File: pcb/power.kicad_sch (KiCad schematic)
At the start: 17 parts, among them Q1 CSD18540Q5B, U1 LM74500-Q1, U2 TVS2700DRV, U3 TPSM33620S5QRDNRQ1, U4 LM1117-Q1-3.3

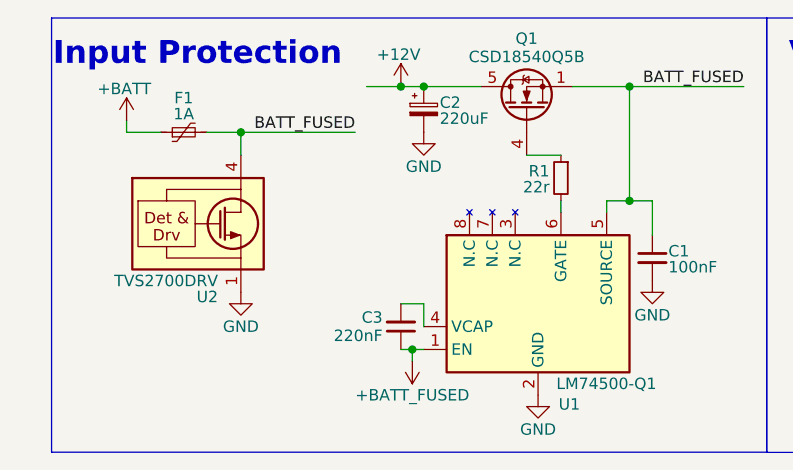
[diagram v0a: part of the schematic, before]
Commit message: pcb gitignore update, netting and mcu pinning
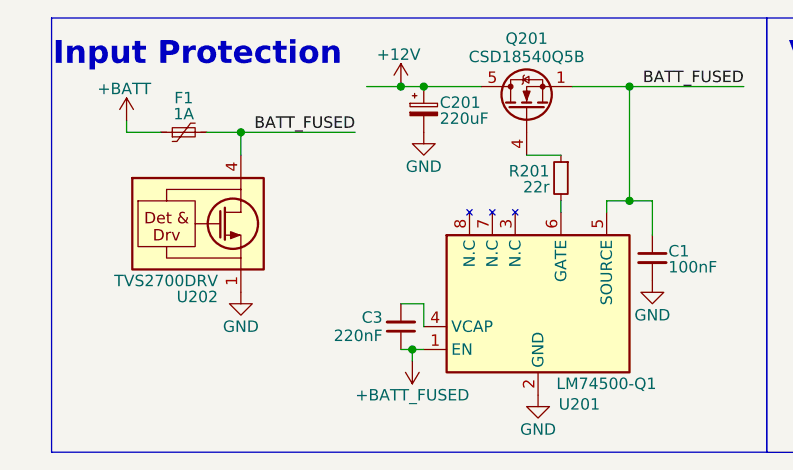
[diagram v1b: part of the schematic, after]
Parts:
- renumbered C2 to C201, Q1 to Q201, R1 to R201, U1 to U201, U2 to U202
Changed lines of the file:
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@@
 		(on_board yes)
 		(dnp no)
-		(property "Reference" "U2"
+		(property "Reference" "U202"
 			(at 33.02 44.958 0)
 			(effects
@@
 			(project "kh_obd2_interface"
 				(path "/0736e313-8db4-41af-b70d-53af7104d2ca/3f40c237-d495-44df-82aa-7228d577e747"
-					(reference "U2")
+					(reference "U202")
 					(unit 1)
 				)
@@
 		(on_board yes)
 		(dnp no)
-		(property "Reference" "R1"
+		(property "Reference" "R201"
 			(at 69.85 30.988 0)
 			(effects
@@
 			(project "kh_obd2_interface"
 				(path "/0736e313-8db4-41af-b70d-53af7104d2ca/3f40c237-d495-44df-82aa-7228d577e747"
-					(reference "R1")
+					(reference "R201")
 					(unit 1)
 				)
@@
 		(on_board yes)
 		(dnp no)
-		(property "Reference" "Q1"
+		(property "Reference" "Q201"
 			(at 67.31 16.256 90)
 			(effects
@@
 			(project "kh_obd2_interface"
 				(path "/0736e313-8db4-41af-b70d-53af7104d2ca/3f40c237-d495-44df-82aa-7228d577e747"
-					(reference "Q1")
+					(reference "Q201")
 					(unit 1)
 				)
@@
 		(on_board yes)
 		(dnp no)
-		(property "Reference" "U1"
+		(property "Reference" "U201"
 			(at 70.866 56.896 0)
 			(effects
@@
 			(project "kh_obd2_interface"
 				(path "/0736e313-8db4-41af-b70d-53af7104d2ca/3f40c237-d495-44df-82aa-7228d577e747"
-					(reference "U1")
+					(reference "U201")
 					(unit 1)
 				)
@@
 		(on_board yes)
 		(dnp no)
-		(property "Reference" "C2"
+		(property "Reference" "C201"
 			(at 57.658 23.368 0)
 			(effects
@@
 			(project "kh_obd2_interface"
 				(path "/0736e313-8db4-41af-b70d-53af7104d2ca/3f40c237-d495-44df-82aa-7228d577e747"
-					(reference "C2")
-					(unit 1)
-				)
+					(reference "C201")
+					(unit 1)
+				)

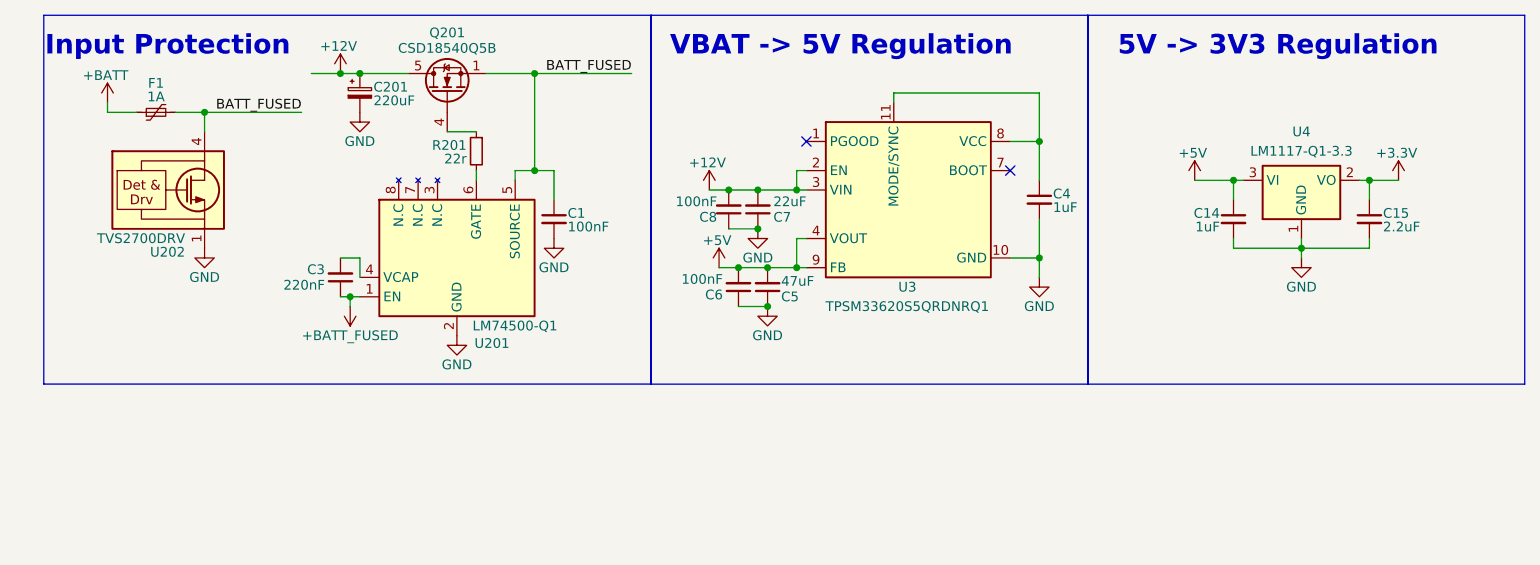
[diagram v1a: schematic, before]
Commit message: add transceivers, routing, drc
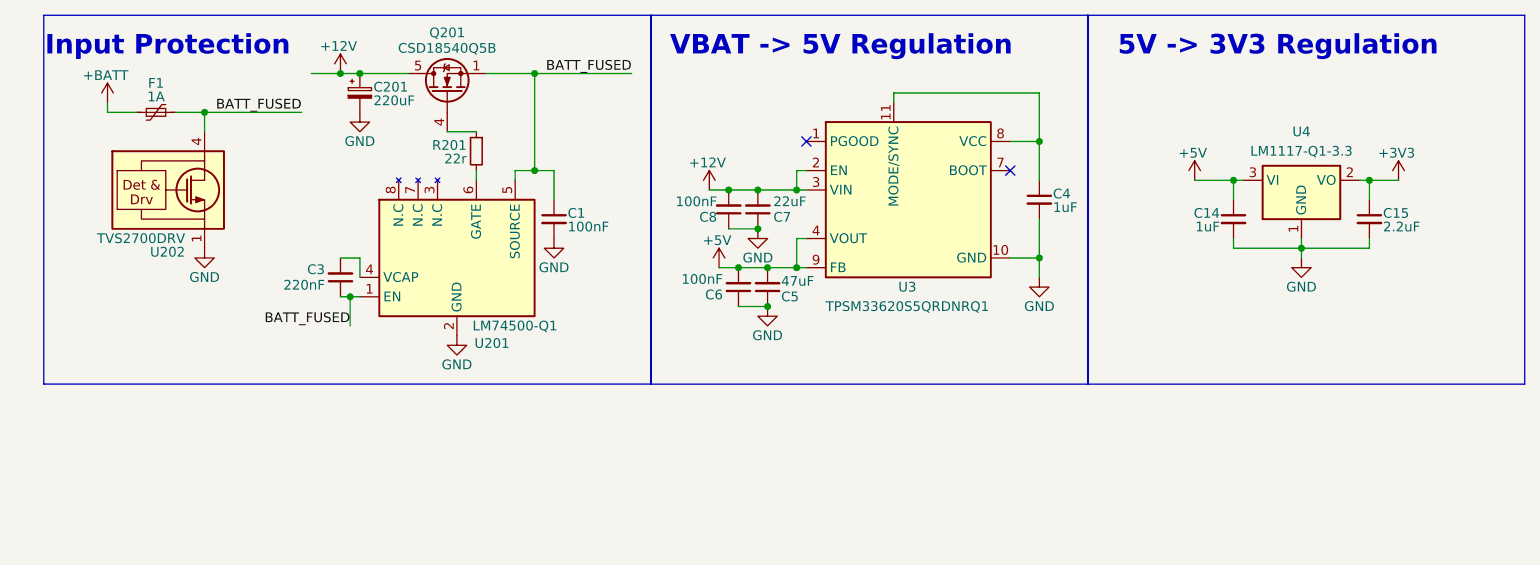
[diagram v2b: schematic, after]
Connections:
- net +BATT_FUSED is gone; now on net BATT_FUSED: C3.1, U201.1 (EN)
- net +3.3V renamed +3V3
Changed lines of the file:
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@@
 	(wire
 		(pts
-			(xy 54.61 50.8) (xy 54.61 52.07)
+			(xy 54.61 50.8) (xy 54.61 54.61)
 		)
 		(stroke
@@
 		)
 	)
+	(label "BATT_FUSED"
+		(at 54.61 54.61 180)
+		(effects
+			(font
+				(size 1.27 1.27)
+			)
+			(justify right bottom)
+		)
+	)
 	(symbol
 		(lib_id "Device:C_Small")
@@
 	(symbol
 		(lib_id "power:+BATT")
-		(at 54.61 52.07 180)
-		(unit 1)
-		(exclude_from_sim no)
-		(in_bom yes)
-		(on_board yes)
-		(dnp no)
-		(property "Reference" "#PWR05"
-			(at 54.61 48.26 0)
-			(effects
-				(font
-					(size 1.27 1.27)
-				)
-				(hide yes)
-			)
-		)
-		(property "Value" "+BATT_FUSED"
-			(at 54.61 55.88 0)
-			(effects
-				(font
-					(size 1.27 1.27)
-				)
-			)
-		)
-		(property "Footprint" ""
-			(at 54.61 52.07 0)
-			(effects
-				(font
-					(size 1.27 1.27)
-				)
-				(hide yes)
-			)
-		)
-		(property "Datasheet" ""
-			(at 54.61 52.07 0)
-			(effects
-				(font
-					(size 1.27 1.27)
-				)
-				(hide yes)
-			)
-		)
-		(property "Description" "Power symbol creates a global label with name \"+BATT\""
-			(at 54.61 52.07 0)
-			(effects
-				(font
-					(size 1.27 1.27)
-				)
-				(hide yes)
-			)
-		)
-		(pin "1"
-		)
-		(instances
-			(project "kh_obd2_interface"
-				(path "/0736e313-8db4-41af-b70d-53af7104d2ca/3f40c237-d495-44df-82aa-7228d577e747"
-					(reference "#PWR05")
-					(unit 1)
-				)
-			)
-		)
-	)
-	(symbol
-		(lib_id "power:+BATT")
 		(at 101.6 36.83 0)
 		(unit 1)
@@
 			)
 		)
-		(property "Value" "+3.3V"
+		(property "Value" "+3V3"
 			(at 191.516 32.004 0)
 			(effects

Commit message: busses are hard
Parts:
- added SW2: SW_SPDT, Connector_PinHeader_2.54mm:PinHeader_1x03_P2.54mm_Vertical_SMD_Pin1Left, symbol Switch:SW_SPDT
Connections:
- net +5V: now also SW2.2 (B); no longer C5.2, C6.2, U3.4 (VOUT), U3.9 (FB)
- new net CAR_5V: C5.2, C6.2, SW2.1 (A), U3.4 (VOUT), U3.9 (FB)
- new net USB_5V: SW2.3 (C)
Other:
- note added: "5V Sourcing Switch"
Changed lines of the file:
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@@
 	(rectangle
 		(start 93.98 13.97)
-		(end 151.1299 62.2299)
+		(end 151.1299 62.23)
 		(stroke
 			(width 0)
@@
 	)
 	(rectangle
-		(start 14.5249 13.97)
-		(end 93.98 62.2151)
+		(start 14.605 13.97)
+		(end 93.98 62.23)
 		(stroke
 			(width 0)
@@
 		(start 151.13 13.97)
 		(end 208.2799 62.2299)
+		(stroke
+			(width 0)
+			(type default)
+		)
+		(fill
+			(type none)
+		)
+	)
+	(rectangle
+		(start 14.605 62.23)
+		(end 54.6099 83.8199)
 		(stroke
 			(width 0)
@@
 		)
 	)
+	(text "5V Sourcing Switch"
+		(exclude_from_sim no)
+		(at 35.052 66.04 0)
+		(effects
+			(font
+				(size 2.54 2.54)
+				(thickness 0.508)
+				(bold yes)
+			)
+		)
+	)
 	(text "Input Protection"
 		(exclude_from_sim no)
@@
 	)
 	(junction
-		(at 53.34 21.59)
-		(diameter 0)
-		(color 0 0 0 0)
-	)
-	(junction
 		(at 113.03 36.83)
 		(diameter 0)
@@
 	(wire
 		(pts
+			(xy 96.52 46.99) (xy 105.41 46.99)
+		)
+		(stroke
+			(width 0)
+			(type default)
+		)
+	)
+	(wire
+		(pts
+			(xy 43.18 73.66) (xy 43.18 77.47)
+		)
+		(stroke
+			(width 0)
+			(type default)
+		)
+	)
+	(wire
+		(pts
 			(xy 53.34 21.59) (xy 55.88 21.59)
 		)
@@
 	(wire
 		(pts
+			(xy 35.56 46.99) (xy 35.56 44.45)
+		)
+		(stroke
+			(width 0)
+			(type default)
+		)
+	)
+	(wire
+		(pts
 			(xy 186.69 35.56) (xy 187.96 35.56)
 		)
@@
 	(wire
 		(pts
-			(xy 102.87 46.99) (xy 105.41 46.99)
+			(xy 26.67 74.93) (xy 29.21 74.93)
 		)
 		(stroke
@@
 	(wire
 		(pts
-			(xy 49.53 21.59) (xy 53.34 21.59)
+			(xy 21.59 80.01) (xy 29.21 80.01)
 		)
 		(stroke
@@
 		(pts
 			(xy 53.34 50.8) (xy 54.61 50.8)
+		)
+		(stroke
+			(width 0)
+			(type default)
+		)
+	)
+	(wire
+		(pts
+			(xy 39.37 77.47) (xy 43.18 77.47)
 		)
 		(stroke
@@
 		)
 	)
+	(label "CAR_5V"
+		(at 96.52 46.99 0)
+		(effects
+			(font
+				(size 1.27 1.27)
+			)
+			(justify left bottom)
+		)
+	)
+	(label "CAR_5V"
+		(at 21.59 80.01 0)
+		(effects
+			(font
+				(size 1.27 1.27)
+			)
+			(justify left bottom)
+		)
+	)
 	(label "BATT_FUSED"
 		(at 48.26 26.67 180)
@@
 		)
 	)
+	(hierarchical_label "USB_5V"
+		(shape input)
+		(at 26.67 74.93 180)
+		(effects
+			(font
+				(size 1.27 1.27)
+			)
+			(justify right)
+		)
+	)
 	(symbol
 		(lib_id "Device:C_Small")
@@
 	(symbol
 		(lib_id "power:+BATT")
-		(at 102.87 46.99 0)
+		(at 43.18 73.66 0)
 		(unit 1)
 		(exclude_from_sim no)
@@
 		(dnp no)
 		(property "Reference" "#PWR019"
-			(at 102.87 50.8 0)
+			(at 43.18 77.47 0)
 			(effects
 				(font
@@
 		)
 		(property "Value" "+5V"
-			(at 102.616 43.434 0)
+			(at 42.926 70.104 0)
 			(effects
 				(font
@@
 		)
 		(property "Footprint" ""
-			(at 102.87 46.99 0)
+			(at 43.18 73.66 0)
 			(effects
 				(font
@@
 		)
 		(property "Datasheet" ""
-			(at 102.87 46.99 0)
+			(at 43.18 73.66 0)
 			(effects
 				(font
@@
 		)
 		(property "Description" "Power symbol creates a global label with name \"+BATT\""
-			(at 102.87 46.99 0)
+			(at 43.18 73.66 0)
 			(effects
 				(font
@@
 	(symbol
 		(lib_id "power:GND")
-		(at 35.56 44.45 0)
+		(at 35.56 46.99 0)
 		(unit 1)
 		(exclude_from_sim no)
@@
 		(dnp no)
 		(property "Reference" "#PWR03"
+			(at 35.56 53.34 0)
+			(effects
+				(font
+					(size 1.27 1.27)
+				)
+				(hide yes)
+			)
+		)
+		(property "Value" "GND"
 			(at 35.56 50.8 0)
 			(effects
@@
 					(size 1.27 1.27)
 				)
-				(hide yes)
-			)
-		)
-		(property "Value" "GND"
-			(at 35.56 48.26 0)
-			(effects
-				(font
-					(size 1.27 1.27)
-				)
 			)
 		)
 		(property "Footprint" ""
-			(at 35.56 44.45 0)
+			(at 35.56 46.99 0)
 			(effects
 				(font
@@
 		)
 		(property "Datasheet" ""
-			(at 35.56 44.45 0)
+			(at 35.56 46.99 0)
 			(effects
 				(font
@@
 		)
 		(property "Description" "Power symbol creates a global label with name \"GND\" , ground"
-			(at 35.56 44.45 0)
+			(at 35.56 46.99 0)
 			(effects
 				(font
@@
 					(unit 1)
 				)
+			)
+		)
+	)
+	(symbol
+		(lib_id "Switch:SW_SPDT")
+		(at 34.29 77.47 180)
+		(unit 1)
+		(exclude_from_sim no)
+		(in_bom yes)
+		(on_board yes)
+		(dnp no)
+		(property "Reference" "SW2"
+			(at 34.29 69.85 0)
+			(effects
+				(font
+					(size 1.27 1.27)
+				)
+			)
+		)
+		(property "Value" "SW_SPDT"
+			(at 34.29 71.882 0)
+			(effects
+				(font
+					(size 1.27 1.27)
+				)
+			)
+		)
+		(property "Footprint" "Connector_PinHeader_2.54mm:PinHeader_1x03_P2.54mm_Vertical_SMD_Pin1Left"
+			(at 34.29 77.47 0)
+			(effects
+				(font
+					(size 1.27 1.27)
+				)
+				(hide yes)
+			)
+		)
+		(property "Datasheet" "~"
+			(at 34.29 69.85 0)
+			(effects
+				(font
+					(size 1.27 1.27)
+				)
+				(hide yes)
+			)
+		)
+		(property "Description" "Switch, single pole double throw"
+			(at 34.29 77.47 0)
+			(effects
+				(font
+					(size 1.27 1.27)
+				)
+				(hide yes)
+			)
+		)
+		(pin "3"
+		)
+		(pin "1"
+		)
+		(pin "2"
+		)
+		(instances
+			(project ""
+				(path "/0736e313-8db4-41af-b70d-53af7104d2ca/3f40c237-d495-44df-82aa-7228d577e747"
+					(reference "SW2")
+					(unit 1)
+				)

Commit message: status/info leds, extra 5v cap
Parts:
- added C4: 47uF, Capacitor_SMD:C_1206_3216Metric, symbol Device:C_Small
- renumbered C14 to C10, C15 to C11, C3 to C2, C4 to C5, C5 to C6, C6 to C7, C7 to C8, C8 to C9
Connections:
- net +5V: now also C4.2
- net GND: now also C4.1

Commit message: connector prep
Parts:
- U3: footprint TIParts:RDN0011A-MFG -> Package_DFN_QFN:Texas_B3QFN-14-1EP_5x5.5mm_P0.65mm_ThermalVia
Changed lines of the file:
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@@
 			)
 		)
-		(property "Footprint" "TIParts:RDN0011A-MFG"
+		(property "Footprint" "Package_DFN_QFN:Texas_B3QFN-14-1EP_5x5.5mm_P0.65mm_ThermalVia"
 			(at 94.488 11.684 0)
 			(effects
